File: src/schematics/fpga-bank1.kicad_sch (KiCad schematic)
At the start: 5 parts, among them U6 LFE5U-85F-*BG756*

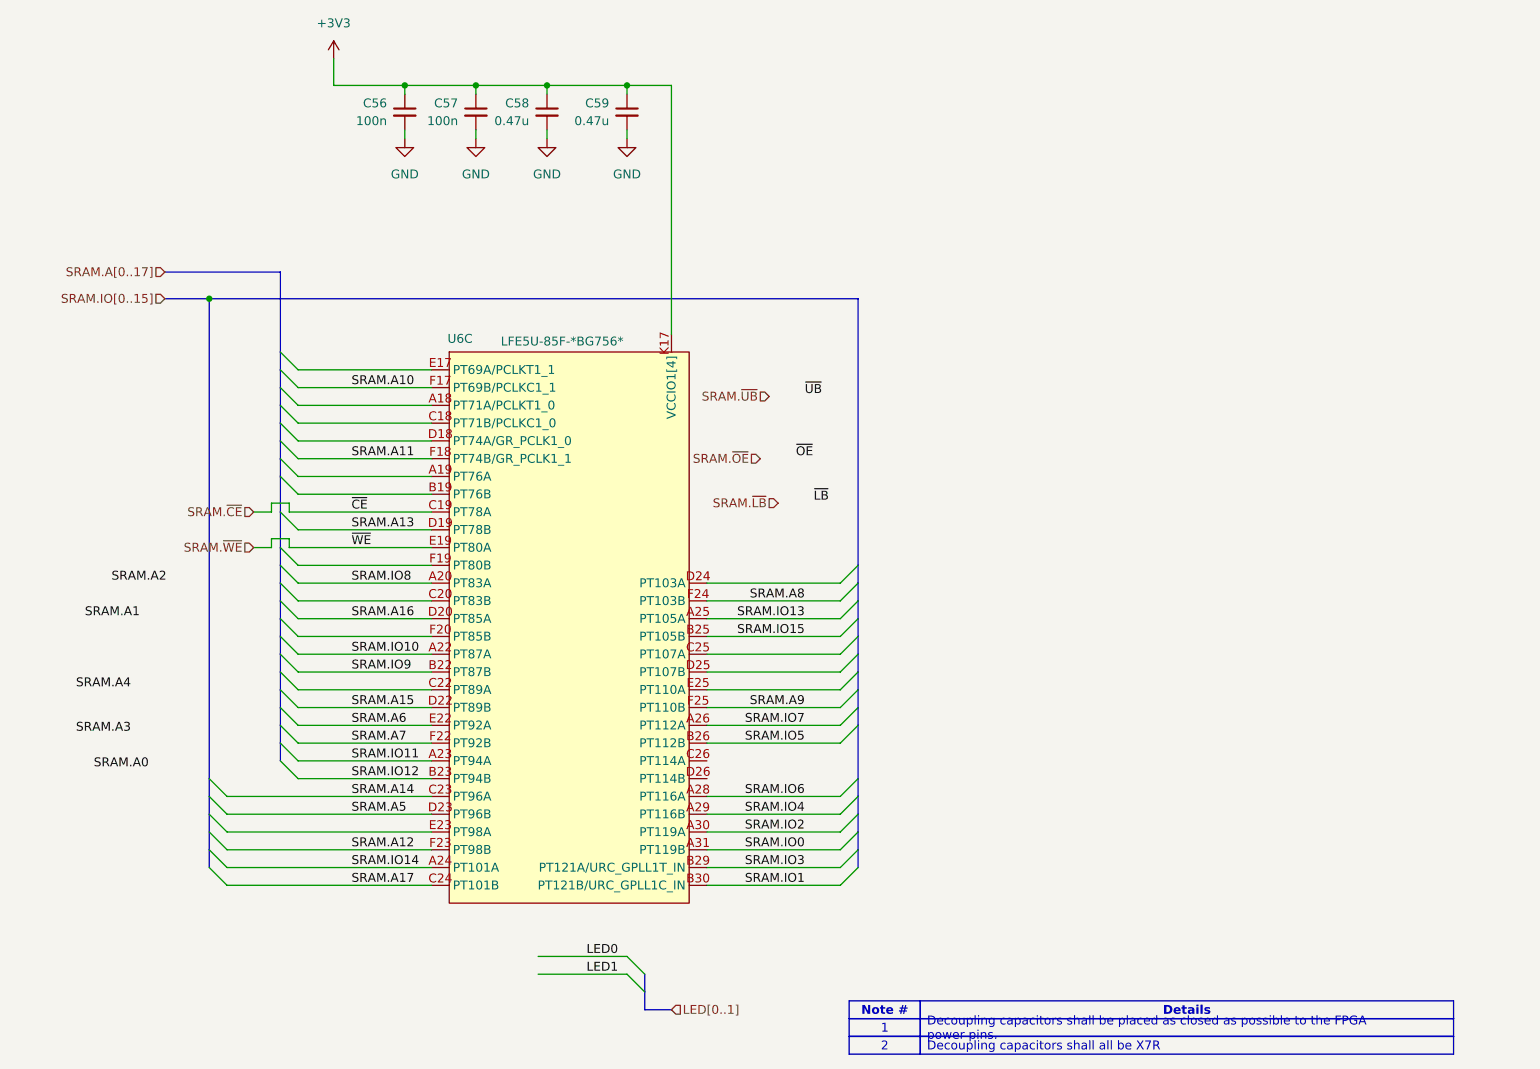
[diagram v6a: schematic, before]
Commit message: Finish routing the SRAM
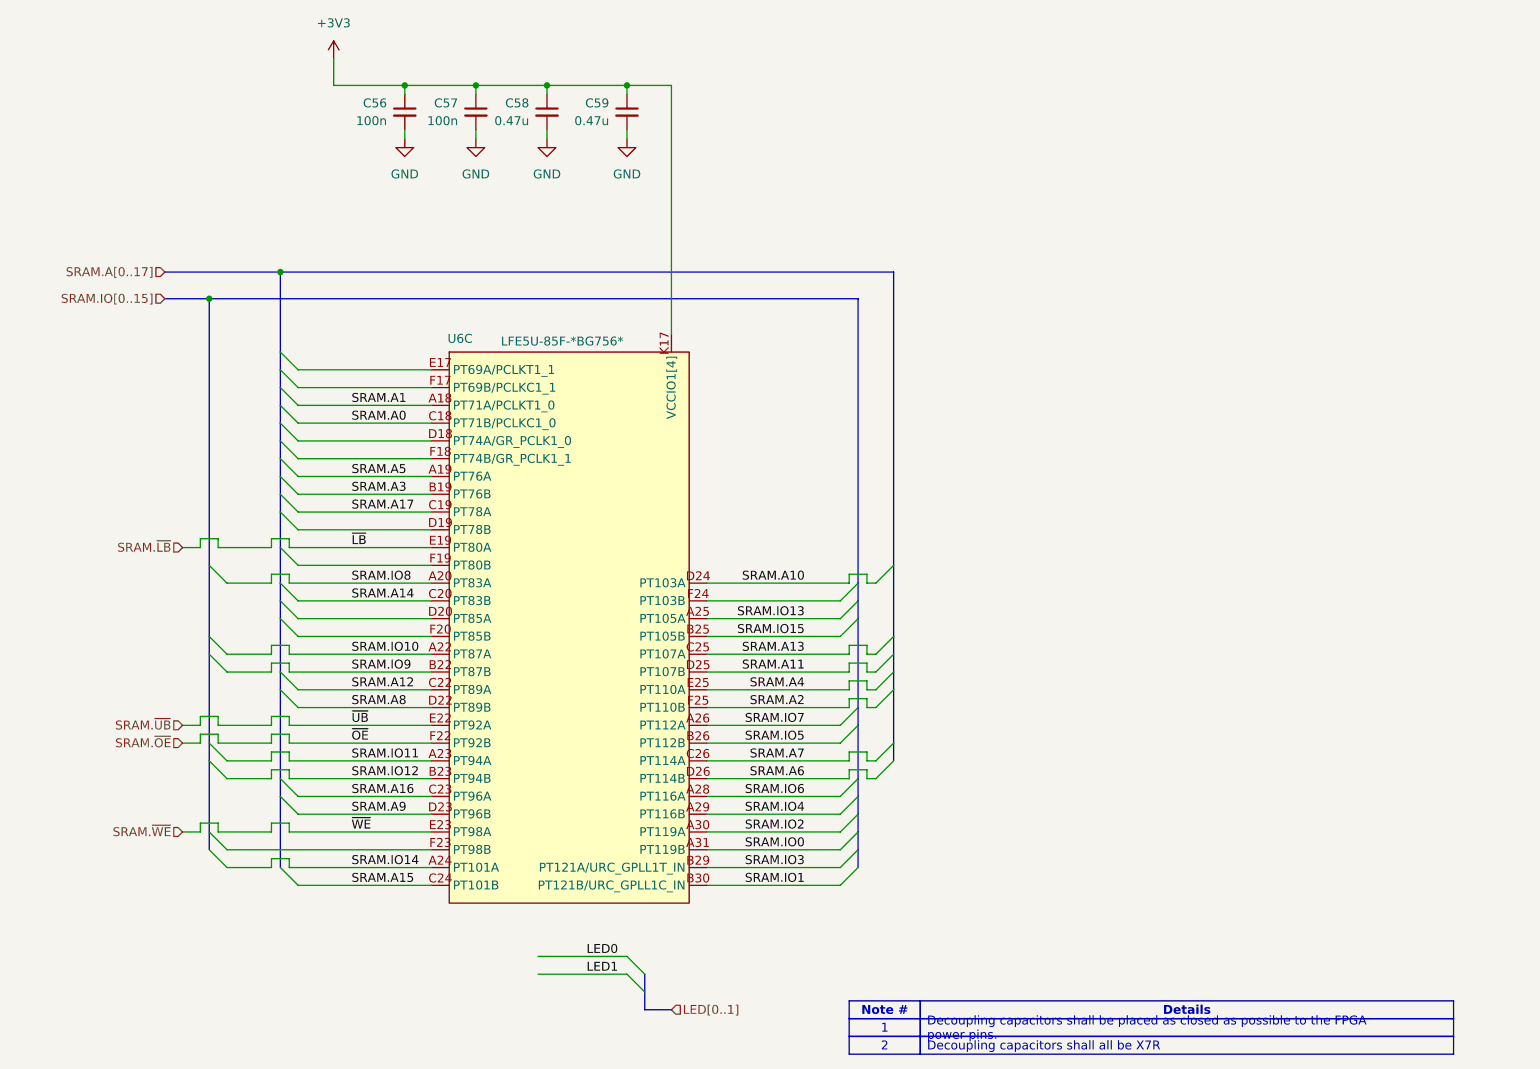
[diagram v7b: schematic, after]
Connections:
- net SRAM.~{CE} is gone; now on net SRAM.A17: U6.C19 (PT78A)
- net SRAM.A0: now also U6.C18 (PT71B/PCLKC1_0)
- net SRAM.A1: now also U6.A18 (PT71A/PCLKT1_0)
- net SRAM.A10: now also U6.D24 (PT103A); no longer U6.F17 (PT69B/PCLKC1_1)
- net SRAM.A11: now also U6.D25 (PT107B); no longer U6.F18 (PT74B/GR_PCLK1_1)
- net SRAM.A12: now also U6.C22 (PT89A); no longer U6.F23 (PT98B)
- net SRAM.A13: now also U6.C25 (PT107A); no longer U6.D19 (PT78B)
- net SRAM.A14: now also U6.C20 (PT83B); no longer U6.C23 (PT96A)
- net SRAM.A15: now also U6.C24 (PT101B); no longer U6.D22 (PT89B)
- net SRAM.A16: now also U6.C23 (PT96A); no longer U6.D20 (PT85A)
- net SRAM.A17: no longer U6.C24 (PT101B)
- net SRAM.A2: now also U6.F25 (PT110B)
- net SRAM.A3: now also U6.B19 (PT76B)
- net SRAM.A4: now also U6.E25 (PT110A)
- net SRAM.A5: now also U6.A19 (PT76A); no longer U6.D23 (PT96B)
- net SRAM.A6: now also U6.D26 (PT114B); no longer U6.E22 (PT92A)
- net SRAM.A7: now also U6.C26 (PT114A); no longer U6.F22 (PT92B)
- net SRAM.A8: now also U6.D22 (PT89B); no longer U6.F24 (PT103B)
- net SRAM.A9: now also U6.D23 (PT96B); no longer U6.F25 (PT110B)
- net SRAM.~{LB}: now also U6.E19 (PT80A)
- net SRAM.~{OE}: now also U6.F22 (PT92B)
- net SRAM.~{UB}: now also U6.E22 (PT92A)
- net SRAM.~{WE}: now also U6.E23 (PT98A); no longer U6.E19 (PT80A)

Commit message: Finish routing the board
* Start updating the power supply routing

* Mirror the connector pinout

* Start routing the connector

* Add second SDRAM chip

* Move decoupling capacitors to the top layer

* Add power monitoring to the schematics

* Start placing the power monitoring

* Start routing the power monitoring

* Add routing of the io connector gnd pins

* Start routing the emmc

* Fix schematic issues

* Finish routing the emmc signals, no length matching

* Fanout the ddr2

* Route the data bus of ddr2

* Route all the DDR2 signals

* Length match the ddr2 data signals

* Fix wrong interpair length matching on ddr2

* Length match the ddr2 L4 signals

* Finished routing the ddr2

* Fix missing via on ddr2 vref

* Add length matching for the emmc

* Route the internal addr bus of sdram

* Start routing the sdram data bus

* Start routing the sdrams

* Find room for sdram signals

* Finish routing the traces for the sdram

* Start assigning signals to pins for sdram

* Start routing the sram

* Cleanup memory schematic

* Apply length matching to the SDRAM

* Start routing the io connector

* fanout the io connector

* Keep routing the io connector

* Start routing the io diff pairs

* Continue routing the io connector

* Finish routing the io connector

* Route more signals in the power supply

* Finish routing all signals

* Fix ERC after routing completion

* Fix wrong annular ring constraint

* Fix DRC issues

* Cleanup tracks

* Fix diff pair skew

* Add stitching vias
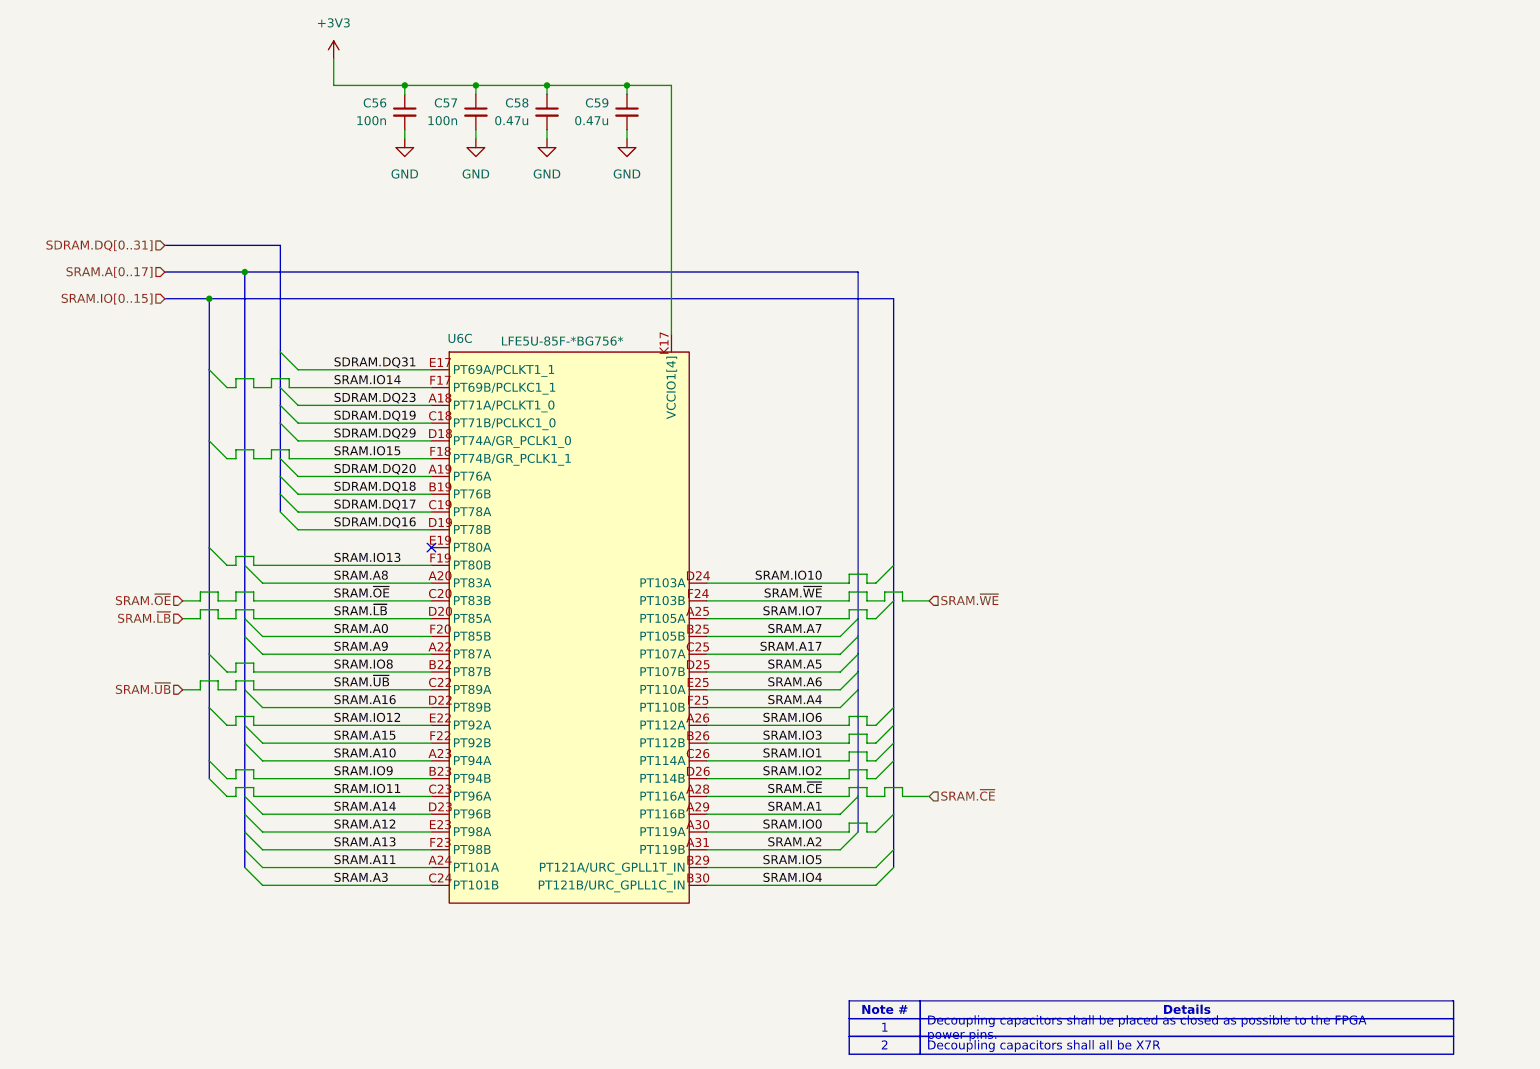
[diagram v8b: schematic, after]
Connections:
- net SRAM.A0: now also U6.F20 (PT85B); no longer U6.C18 (PT71B/PCLKC1_0)
- net SRAM.A1: now also U6.A29 (PT116B); no longer U6.A18 (PT71A/PCLKT1_0)
- net SRAM.A10: now also U6.A23 (PT94A); no longer U6.D24 (PT103A)
- net SRAM.A11: now also U6.A24 (PT101A); no longer U6.D25 (PT107B)
- net SRAM.A12: now also U6.E23 (PT98A); no longer U6.C22 (PT89A)
- net SRAM.A13: now also U6.F23 (PT98B); no longer U6.C25 (PT107A)
- net SRAM.A14: now also U6.D23 (PT96B); no longer U6.C20 (PT83B)
- net SRAM.A15: now also U6.F22 (PT92B); no longer U6.C24 (PT101B)
- net SRAM.A16: now also U6.D22 (PT89B); no longer U6.C23 (PT96A)
- net SRAM.A17: now also U6.C25 (PT107A); no longer U6.C19 (PT78A)
- net SRAM.A2: now also U6.A31 (PT119B); no longer U6.F25 (PT110B)
- net SRAM.A3: now also U6.C24 (PT101B); no longer U6.B19 (PT76B)
- net SRAM.A4: now also U6.F25 (PT110B); no longer U6.E25 (PT110A)
- net SRAM.A5: now also U6.D25 (PT107B); no longer U6.A19 (PT76A)
- net SRAM.A6: now also U6.E25 (PT110A); no longer U6.D26 (PT114B)
- net SRAM.A7: now also U6.B25 (PT105B); no longer U6.C26 (PT114A)
- net SRAM.A8: now also U6.A20 (PT83A); no longer U6.D22 (PT89B)
- net SRAM.A9: now also U6.A22 (PT87A); no longer U6.D23 (PT96B)
- net SRAM.IO0: now also U6.A30 (PT119A); no longer U6.A31 (PT119B)
- net SRAM.IO1: now also U6.C26 (PT114A); no longer U6.B30 (PT121B/URC_GPLL1C_IN)
- net SRAM.IO10: now also U6.D24 (PT103A); no longer U6.A22 (PT87A)
- net SRAM.IO11: now also U6.C23 (PT96A); no longer U6.A23 (PT94A)
- net SRAM.IO12: now also U6.E22 (PT92A); no longer U6.B23 (PT94B)
- net SRAM.IO13: now also U6.F19 (PT80B); no longer U6.A25 (PT105A)
- net SRAM.IO14: now also U6.F17 (PT69B/PCLKC1_1); no longer U6.A24 (PT101A)
- net SRAM.IO15: now also U6.F18 (PT74B/GR_PCLK1_1); no longer U6.B25 (PT105B)
- net SRAM.IO2: now also U6.D26 (PT114B); no longer U6.A30 (PT119A)
- net SRAM.IO3: now also U6.B26 (PT112B); no longer U6.B29 (PT121A/URC_GPLL1T_IN)
- net SRAM.IO4: now also U6.B30 (PT121B/URC_GPLL1C_IN); no longer U6.A29 (PT116B)
- net SRAM.IO5: now also U6.B29 (PT121A/URC_GPLL1T_IN); no longer U6.B26 (PT112B)
- net SRAM.IO6: now also U6.A26 (PT112A); no longer U6.A28 (PT116A)
- net SRAM.IO7: now also U6.A25 (PT105A); no longer U6.A26 (PT112A)
- net SRAM.IO8: now also U6.B22 (PT87B); no longer U6.A20 (PT83A)
- net SRAM.IO9: now also U6.B23 (PT94B); no longer U6.B22 (PT87B)
- net SRAM.~{LB}: now also U6.D20 (PT85A); no longer U6.E19 (PT80A)
- net SRAM.~{OE}: now also U6.C20 (PT83B); no longer U6.F22 (PT92B)
- net SRAM.~{UB}: now also U6.C22 (PT89A); no longer U6.E22 (PT92A)
- net SRAM.~{WE}: now also U6.F24 (PT103B); no longer U6.E23 (PT98A)
- net SDRAM.DQ29: now reaches U6.D18 (PT74A/GR_PCLK1_0)
- net SDRAM.DQ16: now reaches U6.D19 (PT78B)
- net SDRAM.DQ31: now reaches U6.E17 (PT69A/PCLKT1_1)
- new net SDRAM.DQ17: U6.C19 (PT78A)
- new net SDRAM.DQ18: U6.B19 (PT76B)
- new net SDRAM.DQ19: U6.C18 (PT71B/PCLKC1_0)
- new net SDRAM.DQ20: U6.A19 (PT76A)
- new net SDRAM.DQ23: U6.A18 (PT71A/PCLKT1_0)
- new net SRAM.~{CE}: U6.A28 (PT116A)
- no-connect marks 0 -> 1
